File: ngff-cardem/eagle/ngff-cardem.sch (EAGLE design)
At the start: 145 parts, among them IC201 CB3Q3244PW, IC202 CB3Q3244PW, IC203 IP4234CZ6, IC204 FPF2109, IC205 FPF2109, IC301 TPS22958N-DGN, IC302 TPS22958N-DGK, J301 PJ-002BH-SMT-TR, M2 MENTOR_12701001, M3 MENTOR_12701001, Q201 12MHz, T101 BC850, T102 BC850, U201 IP4234CZ6, U202 AT91SAM3S-AU, U301 MIC5366-1.8YC5, X101 PINHD-2X3-SP, X102 ZX360D-B-10P(30), X201 MINI-USB-SHIELD-UX60-MB-5ST, X202 2.54mm, X203 JACK2.5_SJ-2523, X301 171826-4-RA

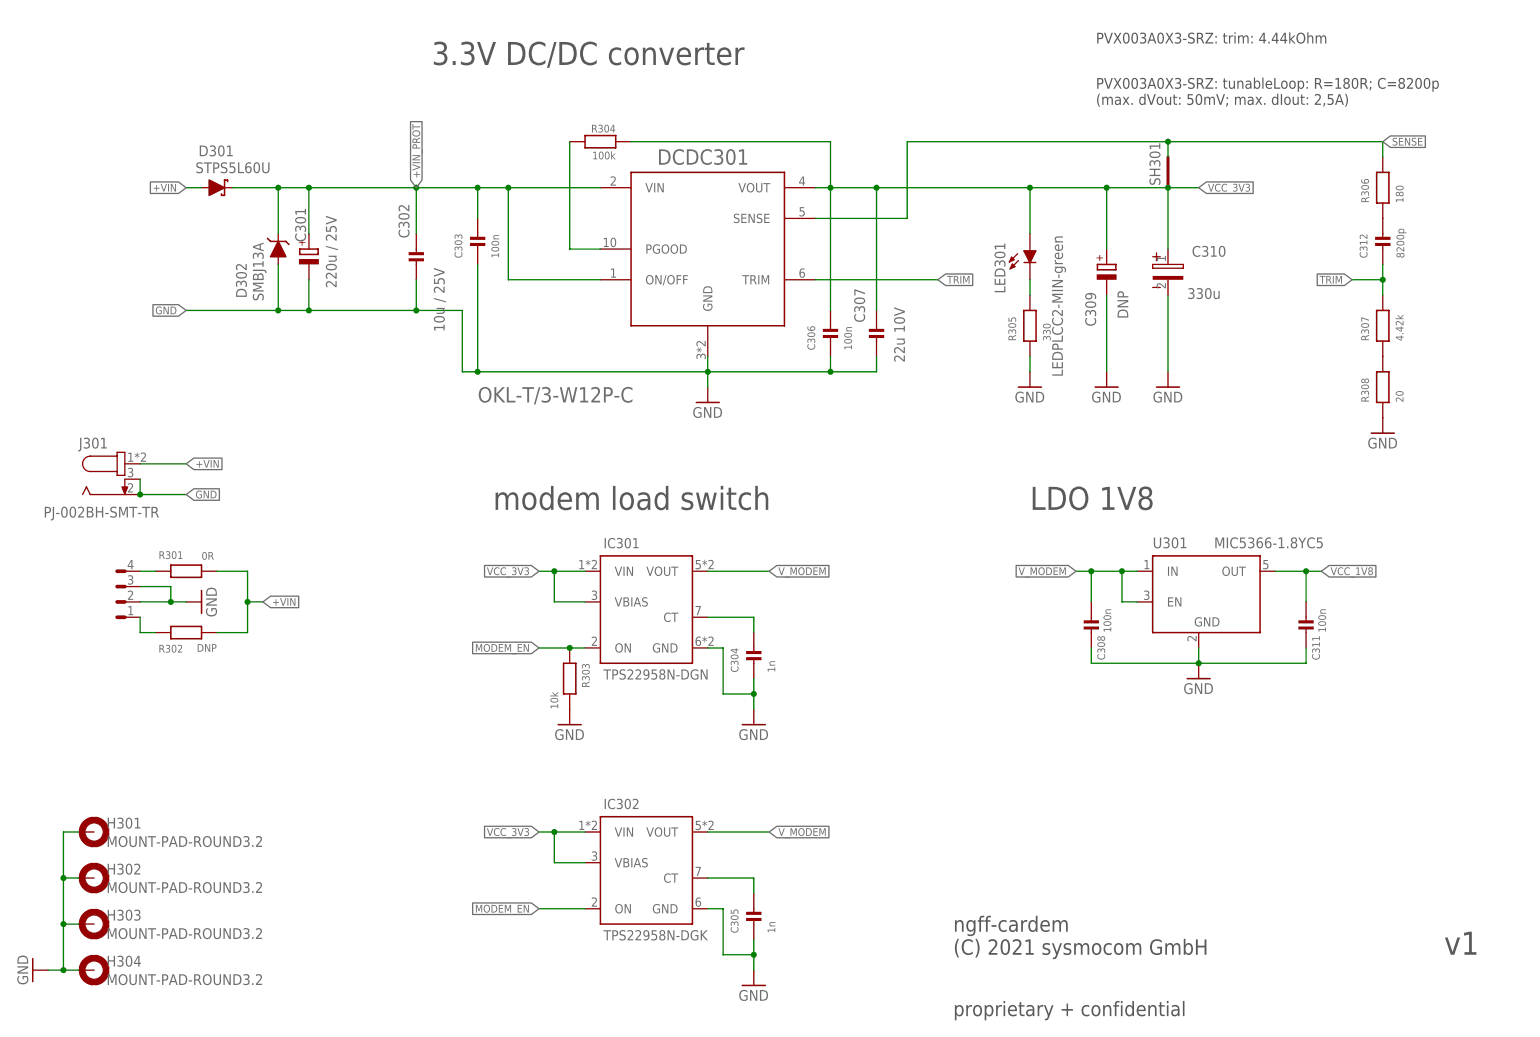
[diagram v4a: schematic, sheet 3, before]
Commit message: ngff-cardem: add PU+PD footpint for DCDC ENA input (solves SYS#5519)
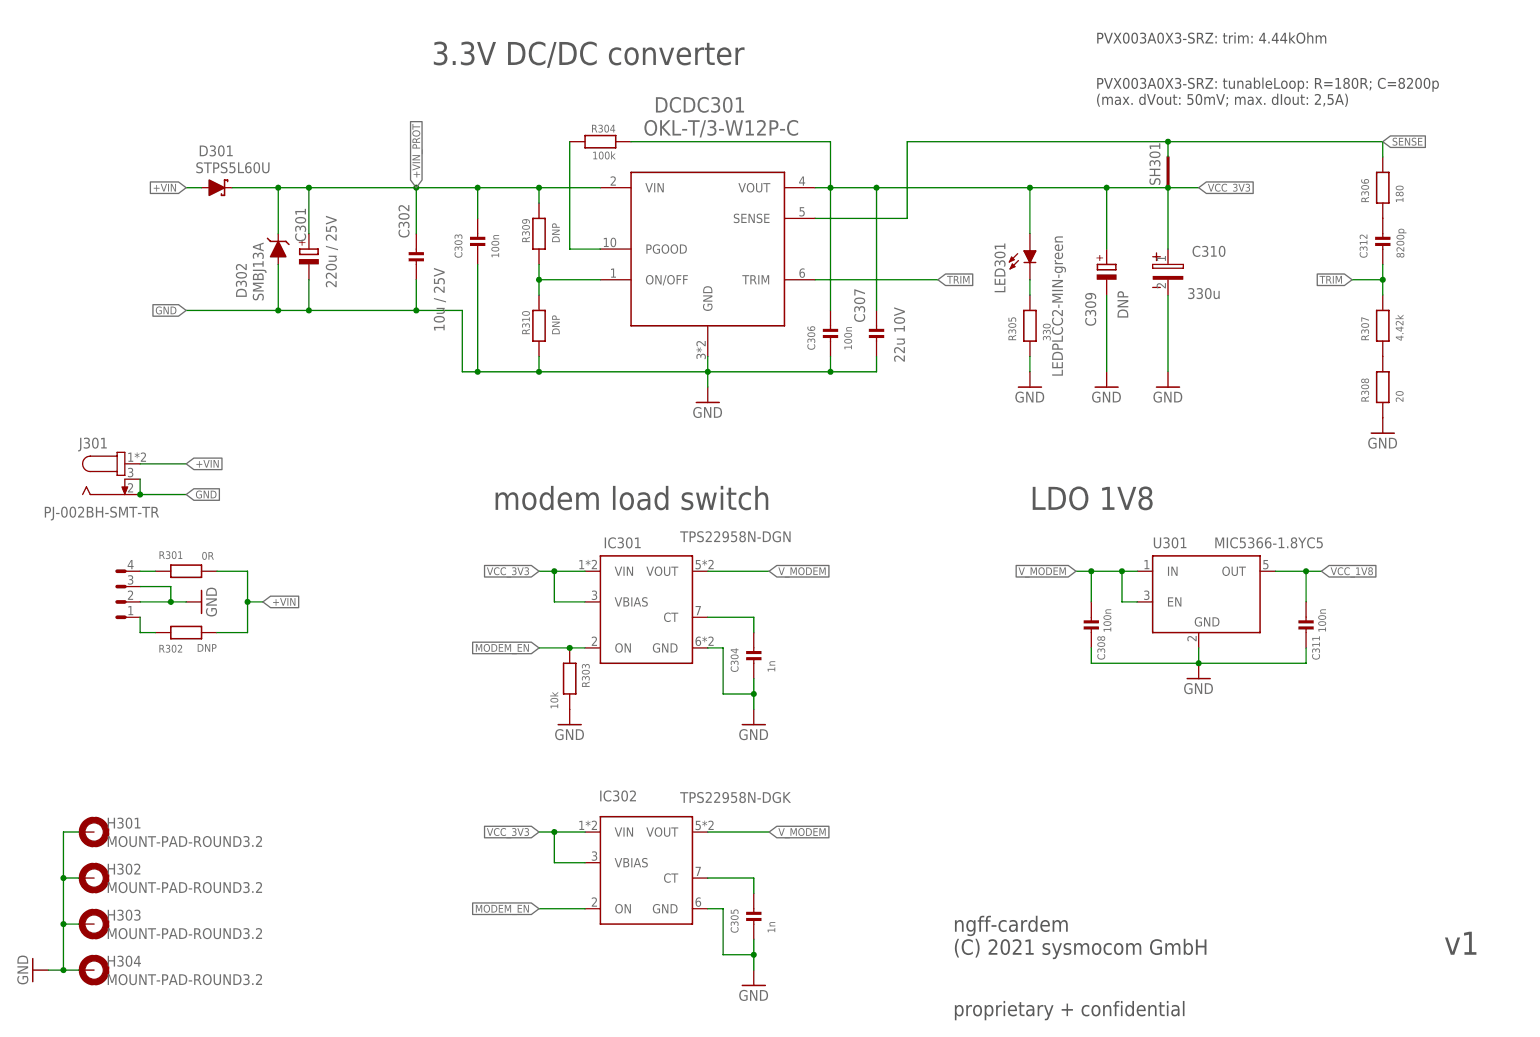
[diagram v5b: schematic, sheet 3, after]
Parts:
- added R309, R310: DNP, rc-sysmocom:RESISTOR_0603
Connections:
- new net N$25: DCDC301.ON/OFF, R309.2, R310.1
- net +VIN_PROT: now also R309.1; no longer DCDC301.ON/OFF
- net GND: now also R310.2
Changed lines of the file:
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@@
 <attribute name="SOURCEPARTNUMBER" value="UNKNOWN SOURCE PART NUMBER"/>
 </part>
+<part name="R309" library="rc-sysmocom" deviceset="RESISTOR" device="_0603" value="DNP">
+<attribute name="CLASS" value="RESISTOR"/>
+<attribute name="DESCRIPTION" value="NO DESCRIPTION"/>
+<attribute name="LINK" value="UNKNOWN LINK"/>
+<attribute name="MANUFACTURER" value="UNKNOWN MANUFACTURER"/>
+<attribute name="MANUFACTURERPARTNUMBER" value="UNKNOWN MANUFACTURER PART NUMBER"/>
+<attribute name="POPULATED" value="FALSE"/>
+<attribute name="ROHSCERTIFICATE" value="UNKNOWN ROHS CERTIFICATE"/>
+<attribute name="SOURCE" value="UNKNOWN SOURCE"/>
+<attribute name="SOURCEPARTNUMBER" value="UNKNOWN SOURCE PART NUMBER"/>
+</part>
+<part name="R310" library="rc-sysmocom" deviceset="RESISTOR" device="_0603" value="DNP">
+<attribute name="CLASS" value="RESISTOR"/>
+<attribute name="DESCRIPTION" value="NO DESCRIPTION"/>
+<attribute name="LINK" value="UNKNOWN LINK"/>
+<attribute name="MANUFACTURER" value="UNKNOWN MANUFACTURER"/>
+<attribute name="MANUFACTURERPARTNUMBER" value="UNKNOWN MANUFACTURER PART NUMBER"/>
+<attribute name="POPULATED" value="FALSE"/>
+<attribute name="ROHSCERTIFICATE" value="UNKNOWN ROHS CERTIFICATE"/>
+<attribute name="SOURCE" value="UNKNOWN SOURCE"/>
+<attribute name="SOURCEPARTNUMBER" value="UNKNOWN SOURCE PART NUMBER"/>
+</part>
 </parts>
 <sheets>
@@
 <wire x1="40.64" y1="101.6" x2="127" y2="101.6" width="0.1524" layer="97" style="longdash"/>
 <wire x1="127" y1="101.6" x2="127" y2="88.9" width="0.1524" layer="97" style="longdash"/>
-<text x="274.32" y="236.22" size="3.81" layer="97" ratio="10" rot="MR180">Console UART</text>
+<text x="294.64" y="223.52" size="3.81" layer="97" ratio="10" rot="MR180">Console UART</text>
 <text x="342.9" y="73.66" size="3.81" layer="97" ratio="10">ADC / version
 detection</text>
@@
 </instance>
 <instance part="DCDC301" gate="G$1" x="281.94" y="238.76" smashed="yes">
-<attribute name="NAME" x="273.558" y="252.73" size="2.54" layer="95"/>
-<attribute name="VALUE" x="243.84" y="213.36" size="2.54" layer="96"/>
+<attribute name="NAME" x="273.05" y="261.366" size="2.54" layer="95"/>
+<attribute name="VALUE" x="271.272" y="257.556" size="2.54" layer="96"/>
 <attribute name="DESCRIPTION" x="281.94" y="238.76" size="1.778" layer="96" display="off"/>
 <attribute name="MANUFACTURER" x="281.94" y="238.76" size="1.778" layer="96" display="off"/>
@@
 </instance>
 <instance part="GND53" gate="1" x="170.18" y="119.38" rot="R270"/>
-<instance part="U301" gate="G$1" x="363.22" y="182.88">
+<instance part="U301" gate="G$1" x="363.22" y="182.88" smashed="yes">
 <attribute name="DESCRIPTION" x="363.22" y="182.88" size="1.778" layer="96" display="off"/>
 <attribute name="MANUFACTURER" x="363.22" y="182.88" size="1.778" layer="96" display="off"/>
@@
 <attribute name="CLASS" x="363.22" y="182.88" size="1.778" layer="96" display="off"/>
 <attribute name="LINK" x="363.22" y="182.88" size="1.778" layer="96" display="off"/>
+<attribute name="NAME" x="355.6" y="189.23" size="1.778" layer="95"/>
+<attribute name="VALUE" x="365.76" y="189.23" size="1.778" layer="96"/>
 </instance>
 <instance part="GND43" gate="1" x="363.22" y="167.64"/>
@@
 <attribute name="CLASS" x="271.78" y="177.8" size="1.778" layer="96" display="off"/>
 <attribute name="LINK" x="271.78" y="177.8" size="1.778" layer="96" display="off"/>
-<attribute name="NAME" x="264.668" y="189.23" size="1.6764" layer="95"/>
-<attribute name="VALUE" x="264.668" y="169.164" size="1.6764" layer="96" align="top-left"/>
+<attribute name="NAME" x="264.668" y="189.23" size="1.778" layer="95"/>
+<attribute name="VALUE" x="277.368" y="192.024" size="1.778" layer="96" align="top-left"/>
 </instance>
 <instance part="GND162" gate="1" x="289.56" y="160.02"/>
@@
 </instance>
 <instance part="IC302" gate="G$1" x="271.78" y="134.62" smashed="yes">
-<attribute name="NAME" x="264.668" y="146.05" size="1.6764" layer="95"/>
-<attribute name="VALUE" x="264.668" y="125.984" size="1.6764" layer="96" align="top-left"/>
+<attribute name="NAME" x="263.906" y="147.32" size="1.778" layer="95"/>
+<attribute name="VALUE" x="277.368" y="148.844" size="1.778" layer="96" align="top-left"/>
 <attribute name="DESCRIPTION" x="271.78" y="134.62" size="1.778" layer="96" display="off"/>
 <attribute name="MANUFACTURER" x="271.78" y="134.62" size="1.778" layer="96" display="off"/>
@@
 <attribute name="VALUE" x="293.116" y="125.476" size="1.27" layer="96" font="vector" rot="R90"/>
 </instance>
+<instance part="R309" gate="G$1" x="254" y="241.3" smashed="yes" rot="R270">
+<attribute name="NAME" x="251.206" y="243.84" size="1.27" layer="95" rot="R270"/>
+<attribute name="VALUE" x="256.159" y="243.078" size="1.27" layer="96" rot="R270"/>
+<attribute name="DESCRIPTION" x="254" y="241.3" size="1.778" layer="96" rot="R270" display="off"/>
+<attribute name="MANUFACTURER" x="254" y="241.3" size="1.778" layer="96" rot="R270" display="off"/>
+<attribute name="MANUFACTURERPARTNUMBER" x="254" y="241.3" size="1.778" layer="96" rot="R270" display="off"/>
+<attribute name="SOURCE" x="254" y="241.3" size="1.778" layer="96" rot="R270" display="off"/>
+<attribute name="SOURCEPARTNUMBER" x="254" y="241.3" size="1.778" layer="96" rot="R270" display="off"/>
+<attribute name="ROHSCERTIFICATE" x="254" y="241.3" size="1.778" layer="96" rot="R270" display="off"/>
+<attribute name="POPULATED" x="254" y="241.3" size="1.778" layer="96" rot="R270" display="off"/>
+<attribute name="CLASS" x="254" y="241.3" size="1.778" layer="96" rot="R270" display="off"/>
+<attribute name="LINK" x="254" y="241.3" size="1.778" layer="96" rot="R270" display="off"/>
+</instance>
+<instance part="R310" gate="G$1" x="254" y="226.06" smashed="yes" rot="R270">
+<attribute name="NAME" x="251.206" y="228.6" size="1.27" layer="95" rot="R270"/>
+<attribute name="VALUE" x="256.159" y="227.838" size="1.27" layer="96" rot="R270"/>
+<attribute name="DESCRIPTION" x="254" y="226.06" size="1.778" layer="96" rot="R270" display="off"/>
+<attribute name="MANUFACTURER" x="254" y="226.06" size="1.778" layer="96" rot="R270" display="off"/>
+<attribute name="MANUFACTURERPARTNUMBER" x="254" y="226.06" size="1.778" layer="96" rot="R270" display="off"/>
+<attribute name="SOURCE" x="254" y="226.06" size="1.778" layer="96" rot="R270" display="off"/>
+<attribute name="SOURCEPARTNUMBER" x="254" y="226.06" size="1.778" layer="96" rot="R270" display="off"/>
+<attribute name="ROHSCERTIFICATE" x="254" y="226.06" size="1.778" layer="96" rot="R270" display="off"/>
+<attribute name="POPULATED" x="254" y="226.06" size="1.778" layer="96" rot="R270" display="off"/>
+<attribute name="CLASS" x="254" y="226.06" size="1.778" layer="96" rot="R270" display="off"/>
+<attribute name="LINK" x="254" y="226.06" size="1.778" layer="96" rot="R270" display="off"/>
+</instance>
 </instances>
 <busses>
@@
 <wire x1="309.88" y1="218.44" x2="309.88" y2="220.98" width="0.1524" layer="91"/>
 <pinref part="DCDC301" gate="G$1" pin="GND"/>
-<wire x1="243.84" y1="218.44" x2="281.94" y2="218.44" width="0.1524" layer="91"/>
+<wire x1="243.84" y1="218.44" x2="254" y2="218.44" width="0.1524" layer="91"/>
+<wire x1="254" y1="218.44" x2="281.94" y2="218.44" width="0.1524" layer="91"/>
 <wire x1="281.94" y1="218.44" x2="281.94" y2="220.98" width="0.1524" layer="91"/>
 <junction x="281.94" y="218.44"/>
@@
 <wire x1="241.3" y1="228.6" x2="241.3" y2="218.44" width="0.1524" layer="91"/>
 <wire x1="241.3" y1="218.44" x2="243.84" y2="218.44" width="0.1524" layer="91"/>
+<pinref part="R310" gate="G$1" pin="2"/>
+<wire x1="254" y1="220.98" x2="254" y2="218.44" width="0.1524" layer="91"/>
+<junction x="254" y="218.44"/>
 </segment>
 <segment>
@@
 <label x="233.68" y="248.92" size="1.27" layer="95" rot="R90" xref="yes"/>
 <pinref part="DCDC301" gate="G$1" pin="VIN"/>
-<wire x1="264.16" y1="248.92" x2="248.92" y2="248.92" width="0.1524" layer="91"/>
+<wire x1="264.16" y1="248.92" x2="254" y2="248.92" width="0.1524" layer="91"/>
 <pinref part="C303" gate="G$1" pin="2"/>
-<wire x1="248.92" y1="248.92" x2="243.84" y2="248.92" width="0.1524" layer="91"/>
+<wire x1="254" y1="248.92" x2="243.84" y2="248.92" width="0.1524" layer="91"/>
 <wire x1="243.84" y1="243.84" x2="243.84" y2="248.92" width="0.1524" layer="91"/>
 <junction x="243.84" y="248.92"/>
-<pinref part="DCDC301" gate="G$1" pin="ON/OFF"/>
-<wire x1="264.16" y1="233.68" x2="248.92" y2="233.68" width="0.1524" layer="91"/>
-<wire x1="248.92" y1="233.68" x2="248.92" y2="248.92" width="0.1524" layer="91"/>
-<junction x="248.92" y="248.92"/>
+<pinref part="R309" gate="G$1" pin="1"/>
+<wire x1="254" y1="246.38" x2="254" y2="248.92" width="0.1524" layer="91"/>
+<junction x="254" y="248.92"/>
 </segment>
 </net>
@@
 </segment>
 </net>
+<net name="N$25" class="3">
+<segment>
+<pinref part="DCDC301" gate="G$1" pin="ON/OFF"/>
+<wire x1="264.16" y1="233.68" x2="254" y2="233.68" width="0.1524" layer="91"/>
+<pinref part="R309" gate="G$1" pin="2"/>
+<wire x1="254" y1="236.22" x2="254" y2="233.68" width="0.1524" layer="91"/>
+<pinref part="R310" gate="G$1" pin="1"/>
+<wire x1="254" y1="231.14" x2="254" y2="233.68" width="0.1524" layer="91"/>
+<junction x="254" y="233.68"/>
+</segment>
+</net>
